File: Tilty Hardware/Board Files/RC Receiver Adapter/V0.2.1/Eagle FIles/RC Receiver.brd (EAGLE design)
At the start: 38.1 x 50.8 mm, 30 parts, among them U1 ATMEGA328P, U2 LM2931, U3 AP7313SOT23R, Y1 16MHz

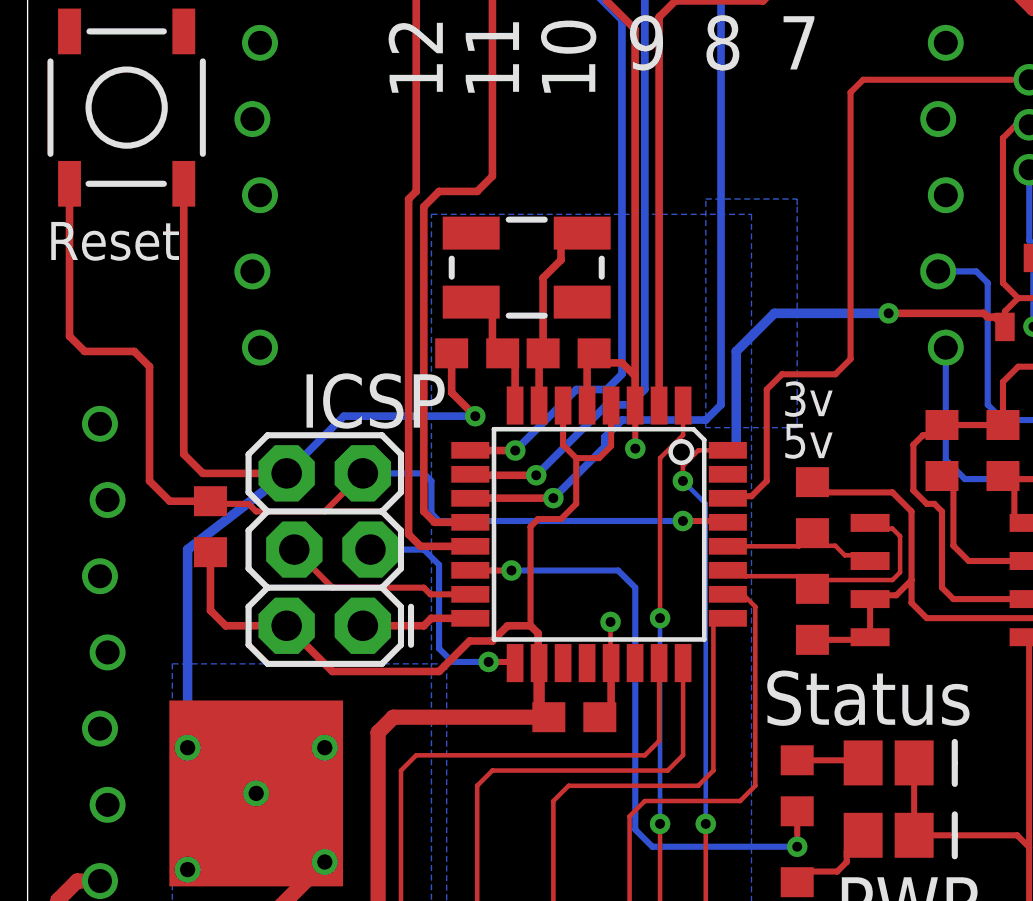
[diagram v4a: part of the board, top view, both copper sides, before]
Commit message: Moved ICSP header to allow for more room to connect a programmer
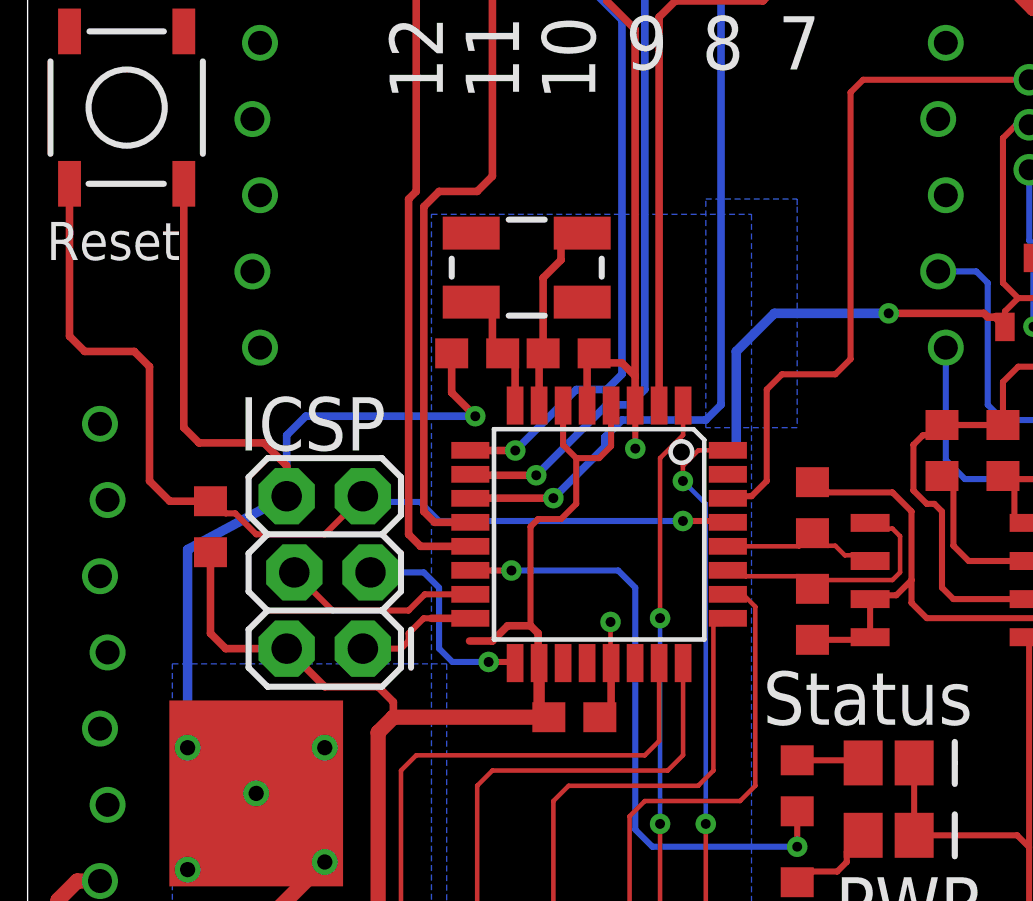
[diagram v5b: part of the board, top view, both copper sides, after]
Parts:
- moved JP6 0.76 mm to (11.2, 21.6)
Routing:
- net +5V: track 171.7 -> 170.1 mm
- net GND: track 188.5 -> 190.0 mm
- net SCK: track 8.02 -> 7.26 mm
- net RESET: track 33.5 -> 32.9 mm
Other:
- board text removed: "3v"
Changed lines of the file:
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@@
 <text x="19.05" y="38.1" size="1.778" layer="26" ratio="12" rot="MR0" align="center">R/C Receiver</text>
 <text x="19.05" y="36.068" size="1.778" layer="26" ratio="12" rot="MR0" align="center">Add-on</text>
-<text x="9.0805" y="28.956" size="1.778" layer="25" ratio="12">ICSP</text>
+<text x="7.0485" y="28.194" size="1.778" layer="25" ratio="12">ICSP</text>
 <text x="26.924" y="12.192" size="1.778" layer="25" ratio="15">PWR</text>
 <text x="0.635" y="34.544" size="1.27" layer="25" ratio="15">Reset</text>
@@
 <text x="11.938" y="48.768" size="1.27" layer="26" ratio="15" rot="MR0">3v3</text>
 <text x="35.56" y="45.72" size="1.27" layer="25" ratio="15" rot="R150">GND</text>
-<text x="25.146" y="27.94" size="1.143" layer="25" ratio="15">5v</text>
-<text x="25.146" y="29.337" size="1.143" layer="25" ratio="15">3v</text>
 </plain>
 <attributes>
@@
 <attribute name="VALUE" x="28.194" y="25.4" size="1.27" layer="27" rot="R90"/>
 </element>
-<element name="JP6" library="SparkFun-Connectors" package="2X3_LOCK" value="AVR_SPI_PRG_62X3_LOCK" x="11.176" y="22.352" smashed="yes" rot="R90"/>
+<element name="JP6" library="SparkFun-Connectors" package="2X3_LOCK" value="AVR_SPI_PRG_62X3_LOCK" x="11.176" y="21.59" smashed="yes" rot="R90"/>
 <element name="JP7" library="My Parts" package="3X6_PTH_HEADER" value="Input" x="18.796" y="4.318" smashed="yes" rot="R180"/>
 <element name="JP8" library="My Parts" package="3-PIN_JST_ZH_CONNECTOR_TH" value="3-PIN_JST_ZH_PTH_CONNECTORRIGHT_ANGLE_PTH" x="34.9885" y="39.0525" rot="R90">
@@
 <wire x1="23.622" y1="31.496" x2="23.622" y2="28.448" width="0.3175" layer="16"/>
 <wire x1="5.334" y1="18.288" x2="5.334" y2="24.892" width="0.3175" layer="16"/>
-<wire x1="5.334" y1="24.892" x2="8.636" y2="27.432" width="0.3175" layer="16"/>
+<wire x1="5.334" y1="24.892" x2="8.636" y2="26.67" width="0.3175" layer="16"/>
 <contactref element="JP2" pad="P$1"/>
 <wire x1="2.667" y1="11.303" x2="4.191" y2="11.303" width="0.508" layer="16"/>
@@
 <contactref element="JP3" pad="P$1"/>
 <contactref element="S1" pad="3"/>
-<wire x1="5.207" y1="28.067" x2="5.207" y2="37.084" width="0.254" layer="1"/>
 <contactref element="D1" pad="2"/>
+<wire x1="5.207" y1="28.956" x2="5.207" y2="37.084" width="0.254" layer="1"/>
 <wire x1="8.167" y1="12.739" x2="8.167" y2="9.0315" width="0.508" layer="1"/>
 <wire x1="8.167" y1="9.0315" x2="6.1205" y2="6.985" width="0.508" layer="1"/>
@@
 <wire x1="8.167" y1="7.239" x2="8.421" y2="6.985" width="0.508" layer="1"/>
 <wire x1="8.382" y1="6.946" x2="8.421" y2="6.985" width="0.508" layer="1"/>
-<wire x1="5.207" y1="28.067" x2="5.842" y2="27.432" width="0.254" layer="1"/>
-<wire x1="5.842" y1="27.432" x2="8.636" y2="27.432" width="0.254" layer="1"/>
 <wire x1="20.25" y1="30.677" x2="20.25" y2="42.234" width="0.254" layer="1"/>
 <wire x1="20.25" y1="42.234" x2="19.304" y2="43.18" width="0.254" layer="1"/>
@@
 <wire x1="14.136" y1="31.4325" x2="14.136" y2="30.1235" width="0.254" layer="1"/>
 <wire x1="14.136" y1="30.1235" x2="14.9225" y2="29.337" width="0.254" layer="1"/>
-<wire x1="14.9225" y1="29.337" x2="10.541" y2="29.337" width="0.254" layer="16"/>
-<wire x1="10.541" y1="29.337" x2="8.636" y2="27.432" width="0.254" layer="16"/>
+<wire x1="14.9225" y1="29.337" x2="9.271" y2="29.337" width="0.254" layer="16"/>
 <contactref element="U$1" pad="P$1"/>
 <via x="19.431" y="22.479" extent="1-16" drill="0.3302"/>
@@
 <wire x1="33.384" y1="11.955" x2="34.036" y2="11.303" width="0.2032" layer="1"/>
 <wire x1="34.036" y1="11.303" x2="35.687" y2="11.303" width="0.2032" layer="1"/>
+<wire x1="8.636" y1="26.67" x2="8.636" y2="27.686" width="0.254" layer="1"/>
+<wire x1="8.636" y1="27.686" x2="7.874" y2="28.448" width="0.254" layer="1"/>
+<wire x1="7.874" y1="28.448" x2="5.715" y2="28.448" width="0.254" layer="1"/>
+<wire x1="5.715" y1="28.448" x2="5.207" y2="28.956" width="0.254" layer="1"/>
+<wire x1="9.271" y1="29.337" x2="8.636" y2="28.702" width="0.254" layer="16"/>
+<wire x1="8.636" y1="28.702" x2="8.636" y2="26.67" width="0.254" layer="16"/>
 <wire x1="18.65" y1="29.6926" x2="14.9225" y2="29.337" width="0" layer="19" extent="1-1"/>
 </signal>
@@
 <wire x1="10.16" y1="6.946" x2="10.121" y2="6.985" width="0.508" layer="1"/>
 <wire x1="15.494" y1="21.844" x2="14.732" y2="21.844" width="0.254" layer="1"/>
-<wire x1="14.732" y1="21.844" x2="13.716" y2="20.828" width="0.254" layer="1"/>
-<wire x1="13.716" y1="20.828" x2="10.16" y2="20.828" width="0.254" layer="1"/>
-<wire x1="10.16" y1="20.828" x2="8.636" y2="22.352" width="0.254" layer="1"/>
-<wire x1="8.636" y1="22.352" x2="6.604" y2="22.352" width="0.254" layer="1"/>
-<wire x1="6.604" y1="22.352" x2="6.096" y2="22.86" width="0.254" layer="1"/>
-<wire x1="6.096" y1="22.86" x2="6.096" y2="24.804" width="0.254" layer="1"/>
+<wire x1="6.096" y1="22.098" x2="6.096" y2="24.804" width="0.254" layer="1"/>
 <contactref element="R5" pad="2"/>
 <contactref element="U$1" pad="P$8"/>
@@
 <wire x1="25.654" y1="12.104" x2="26.758" y2="12.104" width="0.2032" layer="1"/>
 <wire x1="26.758" y1="12.104" x2="29.21" y2="9.652" width="0.2032" layer="1"/>
+<wire x1="6.096" y1="22.098" x2="6.604" y2="21.59" width="0.254" layer="1"/>
+<wire x1="6.604" y1="21.59" x2="8.636" y2="21.59" width="0.254" layer="1"/>
+<wire x1="8.636" y1="21.59" x2="9.906" y2="20.32" width="0.254" layer="1"/>
+<wire x1="9.906" y1="20.32" x2="11.684" y2="20.32" width="0.254" layer="1"/>
+<wire x1="11.684" y1="20.32" x2="12.192" y2="19.812" width="0.254" layer="1"/>
+<wire x1="12.192" y1="19.812" x2="12.192" y2="19.304" width="0.254" layer="1"/>
 </signal>
 <signal name="N$5">
@@
 <contactref element="JP6" pad="1"/>
 <wire x1="14.7574" y1="22.6" x2="13.456" y2="22.6" width="0.254" layer="1"/>
-<wire x1="13.456" y1="22.6" x2="13.208" y2="22.352" width="0.254" layer="1"/>
-<wire x1="13.208" y1="22.352" x2="11.176" y2="22.352" width="0.254" layer="1"/>
+<wire x1="13.456" y1="22.6" x2="13.202" y2="22.6" width="0.2032" layer="1"/>
+<wire x1="13.202" y1="22.6" x2="12.7" y2="22.098" width="0.2032" layer="1"/>
+<wire x1="12.7" y1="22.098" x2="12.7" y2="21.844" width="0.2032" layer="1"/>
+<wire x1="12.7" y1="21.844" x2="12.446" y2="21.59" width="0.2032" layer="1"/>
+<wire x1="12.446" y1="21.59" x2="11.176" y2="21.59" width="0.2032" layer="1"/>
 </signal>
 <signal name="SCK">
@@
 <wire x1="15.367" y1="21.1455" x2="16.2119" y2="21.1455" width="0.2032" layer="1"/>
 <wire x1="16.2119" y1="21.1455" x2="16.25" y2="21.1074" width="0.2032" layer="1"/>
-<wire x1="13.716" y1="21.59" x2="13.716" y2="24.384" width="0.2032" layer="16"/>
-<wire x1="13.716" y1="24.384" x2="13.208" y2="24.892" width="0.2032" layer="16"/>
-<wire x1="13.208" y1="24.892" x2="11.43" y2="24.892" width="0.2032" layer="16"/>
+<wire x1="13.716" y1="21.59" x2="13.716" y2="23.622" width="0.2032" layer="16"/>
+<wire x1="13.716" y1="23.622" x2="13.208" y2="24.13" width="0.2032" layer="16"/>
+<wire x1="13.208" y1="24.13" x2="11.43" y2="24.13" width="0.2032" layer="16"/>
 </signal>
 <signal name="MOSI">
 <contactref element="U1" pad="15"/>
 <contactref element="JP6" pad="4"/>
-<wire x1="14.7574" y1="23.4" x2="13.43" y2="23.4" width="0.2032" layer="1"/>
-<wire x1="13.43" y1="23.4" x2="13.208" y2="23.622" width="0.2032" layer="1"/>
-<wire x1="13.208" y1="23.622" x2="10.16" y2="23.622" width="0.2032" layer="1"/>
-<wire x1="10.16" y1="23.622" x2="8.89" y2="24.892" width="0.2032" layer="1"/>
+<wire x1="14.7574" y1="23.4" x2="13.24" y2="23.4" width="0.2032" layer="1"/>
+<wire x1="13.24" y1="23.4" x2="12.7" y2="22.86" width="0.2032" layer="1"/>
+<wire x1="12.7" y1="22.86" x2="10.16" y2="22.86" width="0.2032" layer="1"/>
+<wire x1="10.16" y1="22.86" x2="8.89" y2="24.13" width="0.2032" layer="1"/>
 </signal>
 <signal name="RESET">
@@
 <wire x1="1.905" y1="31.496" x2="1.397" y2="32.004" width="0.254" layer="1"/>
 <wire x1="1.397" y1="32.004" x2="1.397" y2="37.084" width="0.254" layer="1"/>
-<wire x1="11.176" y1="27.432" x2="13.208" y2="27.432" width="0.2032" layer="16"/>
-<wire x1="13.208" y1="27.432" x2="13.462" y2="27.178" width="0.2032" layer="16"/>
-<wire x1="13.462" y1="27.178" x2="13.462" y2="26.0985" width="0.2032" layer="16"/>
-<wire x1="13.462" y1="26.0985" x2="13.716" y2="25.8445" width="0.2032" layer="16"/>
-<wire x1="6.184" y1="26.416" x2="7.366" y2="26.416" width="0.2032" layer="1"/>
-<wire x1="7.366" y1="26.416" x2="7.62" y2="26.162" width="0.2032" layer="1"/>
-<wire x1="7.62" y1="26.162" x2="9.906" y2="26.162" width="0.2032" layer="1"/>
-<wire x1="9.906" y1="26.162" x2="11.176" y2="27.432" width="0.2032" layer="1"/>
 <wire x1="21.844" y1="25.8445" x2="23.2981" y2="25.8445" width="0.2032" layer="1"/>
 <wire x1="23.2981" y1="25.8445" x2="23.3426" y2="25.8" width="0.2032" layer="1"/>
+<wire x1="6.184" y1="26.416" x2="6.2865" y2="26.416" width="0.2032" layer="1"/>
+<wire x1="6.2865" y1="26.416" x2="6.604" y2="26.0985" width="0.2032" layer="1"/>
+<wire x1="6.604" y1="26.0985" x2="6.9215" y2="26.0985" width="0.2032" layer="1"/>
+<wire x1="6.9215" y1="26.0985" x2="7.62" y2="25.4" width="0.2032" layer="1"/>
+<wire x1="7.62" y1="25.4" x2="9.906" y2="25.4" width="0.2032" layer="1"/>
+<wire x1="9.906" y1="25.4" x2="11.176" y2="26.67" width="0.2032" layer="1"/>
+<wire x1="13.716" y1="25.8445" x2="13.081" y2="26.4795" width="0.2032" layer="16"/>
+<wire x1="13.081" y1="26.4795" x2="11.3665" y2="26.4795" width="0.2032" layer="16"/>
+<wire x1="11.3665" y1="26.4795" x2="11.176" y2="26.67" width="0.2032" layer="16"/>
 </signal>
 <signal name="RC_IN1">

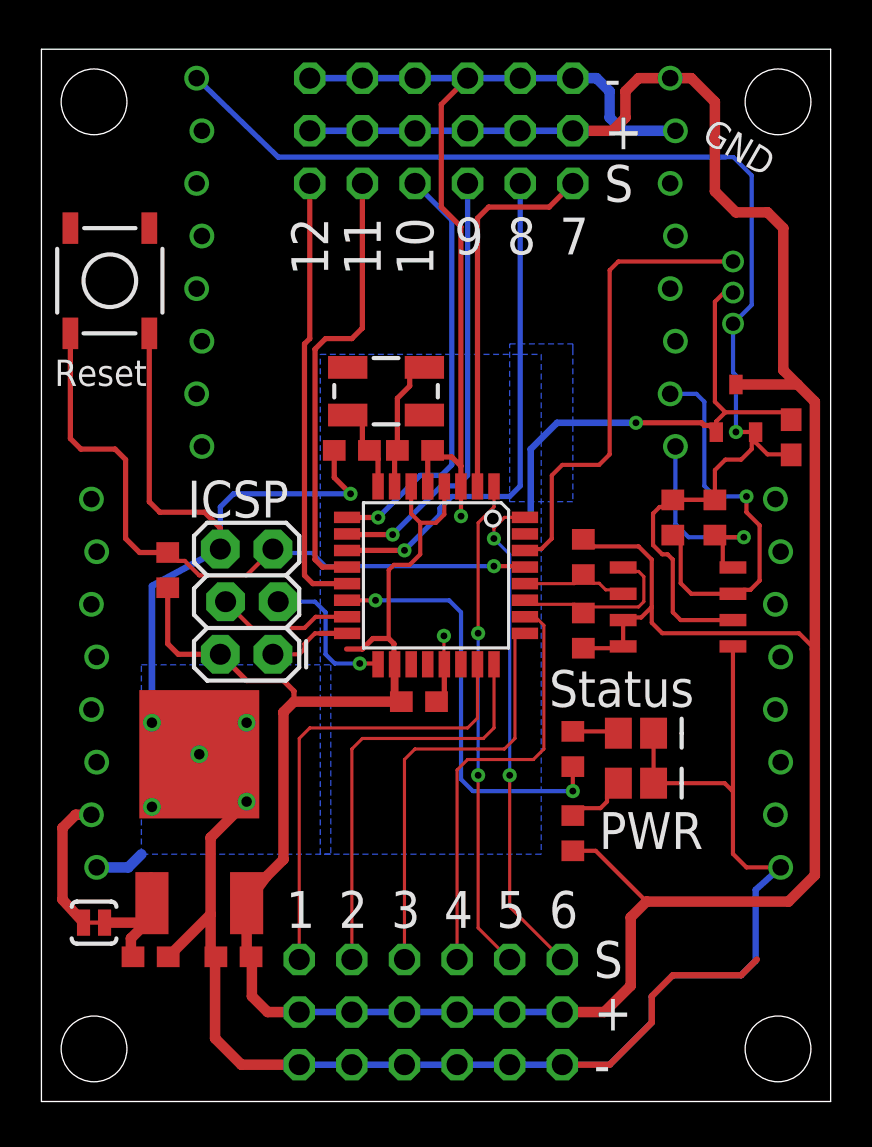
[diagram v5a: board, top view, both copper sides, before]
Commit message: Added Tilty silkscreen and option 5/3.3v I2C connections
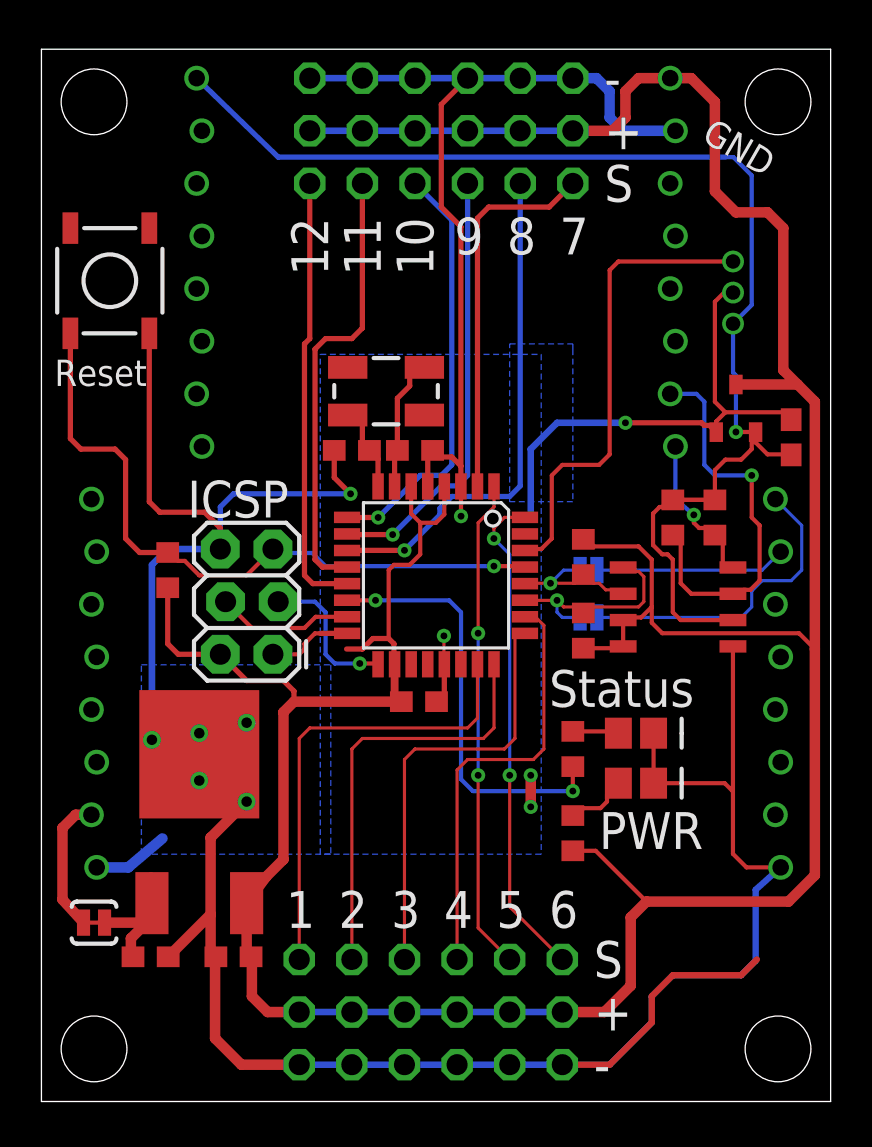
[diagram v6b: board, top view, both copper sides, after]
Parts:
- added SJ2, SJ3: SOLDERJUMPERNC2, SparkFun-Passives:SJ_2S-NOTRACE
- renumbered U$1 to U4
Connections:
- new net N$7: JP3.P$8, SJ3.1
- new net N$8: JP3.P$7, SJ2.1
- net 5V_SCL: now also SJ2.2
- net 5V_SDA: now also SJ3.2
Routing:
- net N$7: track 0.00 -> 15.2 mm
- net N$8: track 0.00 -> 9.24 mm
- net GND: track 190.0 -> 194.5 mm, vias 9 -> 11
- net 3V_SDA: track 11.5 -> 8.23 mm
- net 5V_SDA: track 8.61 -> 10.4 mm, vias 0 -> 1
- net 5V_SCL: track 5.31 -> 7.01 mm, vias 0 -> 1
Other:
- board text added: "0"
- board text added: "13"
- board text added: "14"
- board text added: "15"
- board text added: "16"
- board text added: "17"
- board text added: "18"
- board text added: "19"
- board text added: "20"
- board text added: "21"
- board text added: "22"
- board text added: "23"
- board text added: "ASCL"
- board text added: "ASDA"
- board text added: "Vin"
